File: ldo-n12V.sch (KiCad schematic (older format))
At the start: 0 parts

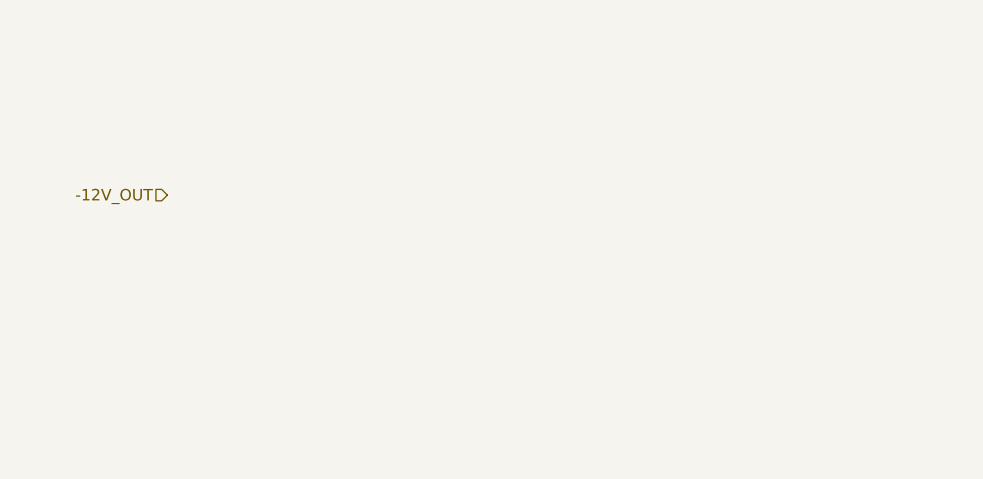
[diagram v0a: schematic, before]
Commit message: add schematics for LDO sheets
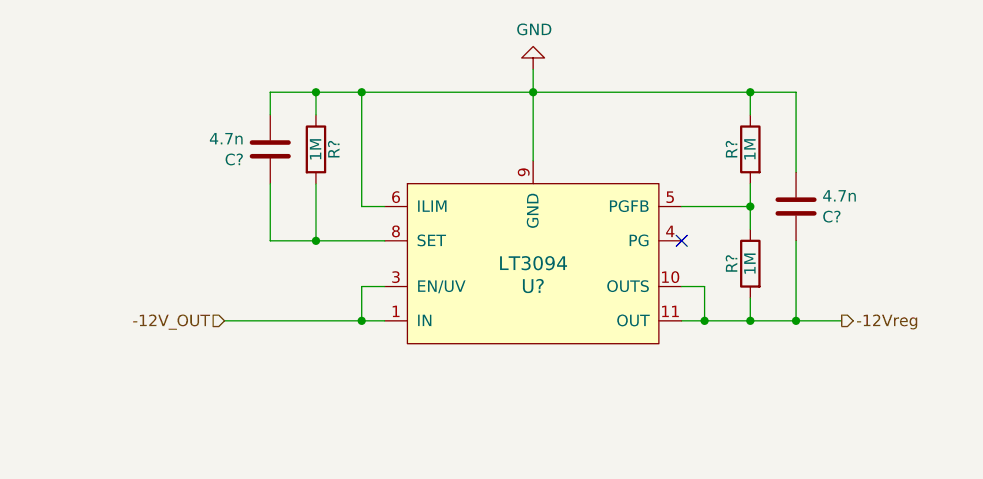
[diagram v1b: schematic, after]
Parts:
- added C? (x2): 4.7n, Capacitor_SMD:C_0805_2012Metric_Pad1.15x1.40mm_HandSolder, symbol Device:C
- added R? (x3): 1M, Resistor_SMD:R_0805_2012Metric_Pad1.15x1.40mm_HandSolder, symbol Device:R
- added U?: LT3094, Housings_SSOP:MSOP-12-1EP_3x4mm_Pitch0.65mm, symbol linear_technology:LT3094
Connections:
- new net: C?.2, R?.2, U?.8 (SET)
- new net: R?.1, R?.2, U?.5 (PGFB)
- new net -12Vreg: C?.2, R?.2, U?.10 (OUTS), U?.11 (OUT), U?.12 (OUT)
- new net GND: C?.1, C?.1, R?.1, R?.1, U?.6 (ILIM), U?.9 (GND)
- new net IN: U?.1 (IN), U?.13 (IN), U?.2 (IN), U?.3 (EN/UV)
- no-connect marks 0 -> 1
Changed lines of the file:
@@
 Comment4 ""
 $EndDescr
-Text HLabel 4300 4150 0    50   Input ~ 0
+Text HLabel 4550 4700 0    50   Input ~ 0
 -12V_OUT
+NoConn ~ 6550 4350
+$Comp
+L power:GND #PWR?
+U 1 1 5CA61EBE
+P 5900 3600
+AR Path="/5C903B7C/5CA61EBE" Ref="#PWR?"  Part="1"
+AR Path="/5CA59CF7/5CA61EBE" Ref="#PWR?"  Part="1"
+F 0 "#PWR?" H 5900 3350 50  0001 C CNN
+F 1 "GND" H 5905 3427 50  0000 C CNN
+F 2 "" H 5900 3600 50  0001 C CNN
+F 3 "" H 5900 3600 50  0001 C CNN
+	1    5900 3600
+	1    0    0    1
+$EndComp
+Wire Wire Line
+	5900 3600 5900 3700
+Wire Wire Line
+	5250 4200 5150 4200
+Wire Wire Line
+	5150 4200 5150 3700
+Wire Wire Line
+	5150 3700 5900 3700
+Connection ~ 5900 3700
+Wire Wire Line
+	5900 3700 5900 4000
+Wire Wire Line
+	4550 4700 5150 4700
+Wire Wire Line
+	5150 4700 5150 4550
+Wire Wire Line
+	5150 4550 5250 4550
+Connection ~ 5150 4700
+Wire Wire Line
+	5150 4700 5250 4700
+$Comp
+L Device:R R?
+U 1 1 5CA61ED4
+P 4950 3950
+AR Path="/5C87B3B6/5CA61ED4" Ref="R?"  Part="1"
+AR Path="/5CA59CF7/5CA61ED4" Ref="R?"  Part="1"
+F 0 "R?" V 5030 3950 50  0000 C CNN
+F 1 "1M" V 4950 3950 50  0000 C CNN
+F 2 "Resistor_SMD:R_0805_2012Metric_Pad1.15x1.40mm_HandSolder" V 4880 3950 50  0001 C CNN
+F 3 "https://industrial.panasonic.com/cdbs/www-data/pdf/RDA0000/AOA0000C304.pdf" H 4950 3950 50  0001 C CNN
+F 4 "RES SMD 1M OHM 1% 1/8W 0805" H 4950 3950 50  0001 C CNN "Description"
+F 5 "Panasonic Electronic Components" H 4950 3950 50  0001 C CNN "Manufacturer"
+F 6 "ERJ-6ENF1004V" H 4950 3950 50  0001 C CNN "Manufacturer Part Number"
+F 7 "Digi-Key" H 4950 3950 50  0001 C CNN "Supplier"
+F 8 "P1.00MCCT-ND" H 4950 3950 50  0001 C CNN "Supplier Part Number"
+	1    4950 3950
+	1    0    0    -1
+$EndComp
+$Comp
+L Device:C C?
+U 1 1 5CA61EE0
+P 4750 3950
+AR Path="/5C87B3B6/5CA61EE0" Ref="C?"  Part="1"
+AR Path="/5CA59CF7/5CA61EE0" Ref="C?"  Part="1"
+F 0 "C?" H 4635 3904 50  0000 R CNN
+F 1 "4.7n" H 4635 3995 50  0000 R CNN
+F 2 "Capacitor_SMD:C_0805_2012Metric_Pad1.15x1.40mm_HandSolder" H 4788 3800 50  0001 C CNN
+F 3 "http://www.samsungsem.com/kr/support/product-search/mlcc/__icsFiles/afieldfile/2018/06/12/CL21C4R7BBANNNC.pdf" H 4750 3950 50  0001 C CNN
+F 4 "CAP CER 4.7PF 50V C0G/NP0 0805" H 2300 -1200 50  0001 C CNN "Description"
+F 5 "Samsung Electro-Mechanics" H 2300 -1200 50  0001 C CNN "Manufacturer"
+F 6 "CL21C4R7BBANNNC" H 2300 -1200 50  0001 C CNN "Manufacturer Part Number"
+F 7 "Digi-Key" H 2300 -1200 50  0001 C CNN "Supplier"
+F 8 "1276-1832-1-ND" H 2300 -1200 50  0001 C CNN "Supplier Part Number"
+	1    4750 3950
+	1    0    0    -1
+$EndComp
+Wire Wire Line
+	5250 4350 4950 4350
+Wire Wire Line
+	4750 4350 4750 4100
+Wire Wire Line
+	4950 4350 4950 4100
+Connection ~ 4950 4350
+Wire Wire Line
+	4950 4350 4750 4350
+Wire Wire Line
+	4750 3800 4750 3700
+Wire Wire Line
+	4750 3700 4950 3700
+Connection ~ 5150 3700
+Wire Wire Line
+	4950 3800 4950 3700
+Connection ~ 4950 3700
+Wire Wire Line
+	4950 3700 5150 3700
+$Comp
+L Device:R R?
+U 1 1 5CA61EF7
+P 6850 3950
+AR Path="/5C87B3B6/5CA61EF7" Ref="R?"  Part="1"
+AR Path="/5CA59CF7/5CA61EF7" Ref="R?"  Part="1"
+F 0 "R?" V 6930 3950 50  0000 C CNN
+F 1 "1M" V 6850 3950 50  0000 C CNN
+F 2 "Resistor_SMD:R_0805_2012Metric_Pad1.15x1.40mm_HandSolder" V 6780 3950 50  0001 C CNN
+F 3 "https://industrial.panasonic.com/cdbs/www-data/pdf/RDA0000/AOA0000C304.pdf" H 6850 3950 50  0001 C CNN
+F 4 "RES SMD 1M OHM 1% 1/8W 0805" H 6850 3950 50  0001 C CNN "Description"
+F 5 "Panasonic Electronic Components" H 6850 3950 50  0001 C CNN "Manufacturer"
+F 6 "ERJ-6ENF1004V" H 6850 3950 50  0001 C CNN "Manufacturer Part Number"
+F 7 "Digi-Key" H 6850 3950 50  0001 C CNN "Supplier"
+F 8 "P1.00MCCT-ND" H 6850 3950 50  0001 C CNN "Supplier Part Number"
+	1    6850 3950
+	-1   0    0    -1
+$EndComp
+$Comp
+L Device:R R?
+U 1 1 5CA61F03
+P 6850 4450
+AR Path="/5C87B3B6/5CA61F03" Ref="R?"  Part="1"
+AR Path="/5CA59CF7/5CA61F03" Ref="R?"  Part="1"
+F 0 "R?" V 6930 4450 50  0000 C CNN
+F 1 "1M" V 6850 4450 50  0000 C CNN
+F 2 "Resistor_SMD:R_0805_2012Metric_Pad1.15x1.40mm_HandSolder" V 6780 4450 50  0001 C CNN
+F 3 "https://industrial.panasonic.com/cdbs/www-data/pdf/RDA0000/AOA0000C304.pdf" H 6850 4450 50  0001 C CNN
+F 4 "RES SMD 1M OHM 1% 1/8W 0805" H 6850 4450 50  0001 C CNN "Description"
+F 5 "Panasonic Electronic Components" H 6850 4450 50  0001 C CNN "Manufacturer"
+F 6 "ERJ-6ENF1004V" H 6850 4450 50  0001 C CNN "Manufacturer Part Number"
+F 7 "Digi-Key" H 6850 4450 50  0001 C CNN "Supplier"
+F 8 "P1.00MCCT-ND" H 6850 4450 50  0001 C CNN "Supplier Part Number"
+	1    6850 4450
+	-1   0    0    -1
+$EndComp
+Wire Wire Line
+	6550 4200 6850 4200
+Wire Wire Line
+	6850 4200 6850 4300
+Wire Wire Line
+	6550 4700 6650 4700
+Wire Wire Line
+	6850 4700 6850 4600
+Wire Wire Line
+	6550 4550 6650 4550
+Wire Wire Line
+	6650 4550 6650 4700
+Connection ~ 6650 4700
+Wire Wire Line
+	6650 4700 6850 4700
+Wire Wire Line
+	6850 4200 6850 4100
+Connection ~ 6850 4200
+Wire Wire Line
+	6850 3800 6850 3700
+Wire Wire Line
+	6850 3700 5900 3700
+$Comp
+L Device:C C?
+U 1 1 5CA61F1B
+P 7050 4200
+AR Path="/5C87B3B6/5CA61F1B" Ref="C?"  Part="1"
+AR Path="/5CA59CF7/5CA61F1B" Ref="C?"  Part="1"
+F 0 "C?" H 6935 4154 50  0000 R CNN
+F 1 "4.7n" H 6935 4245 50  0000 R CNN
+F 2 "Capacitor_SMD:C_0805_2012Metric_Pad1.15x1.40mm_HandSolder" H 7088 4050 50  0001 C CNN
+F 3 "http://www.samsungsem.com/kr/support/product-search/mlcc/__icsFiles/afieldfile/2018/06/12/CL21C4R7BBANNNC.pdf" H 7050 4200 50  0001 C CNN
+F 4 "CAP CER 4.7PF 50V C0G/NP0 0805" H 4600 -950 50  0001 C CNN "Description"
+F 5 "Samsung Electro-Mechanics" H 4600 -950 50  0001 C CNN "Manufacturer"
+F 6 "CL21C4R7BBANNNC" H 4600 -950 50  0001 C CNN "Manufacturer Part Number"
+F 7 "Digi-Key" H 4600 -950 50  0001 C CNN "Supplier"
+F 8 "1276-1832-1-ND" H 4600 -950 50  0001 C CNN "Supplier Part Number"
+	1    7050 4200
+	-1   0    0    -1
+$EndComp
+Wire Wire Line
+	6850 4700 7050 4700
+Wire Wire Line
+	7050 4700 7050 4350
+Connection ~ 6850 4700
+Wire Wire Line
+	7050 4050 7050 3700
+Wire Wire Line
+	7050 3700 6850 3700
+Connection ~ 6850 3700
+Text HLabel 7250 4700 2    50   Output ~ 0
+-12Vreg
+Wire Wire Line
+	7250 4700 7050 4700
+Connection ~ 7050 4700
+$Comp
+L linear_technology:LT3094 U?
+U 1 1 5CA624E4
+P 5900 4450
+F 0 "U?" H 5900 4350 60  0000 C CNN
+F 1 "LT3094" H 5900 4450 60  0000 C CNN
+F 2 "Housings_SSOP:MSOP-12-1EP_3x4mm_Pitch0.65mm" H 5900 3950 60  0001 C CNN
+F 3 "https://www.analog.com/media/en/technical-documentation/data-sheets/LT3094.pdf" H 5900 4050 60  0001 C CNN
+	1    5900 4450
+	1    0    0    -1
+$EndComp
 $EndSCHEMATC

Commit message: update schematic after LTSpice simulations
- enable EN/UV and PGFB usage for LDOs
  - PGFB required for fast startup
  - EN/UV required to allow boost to ramp up
- take care of some TODOs in usbc-power sch
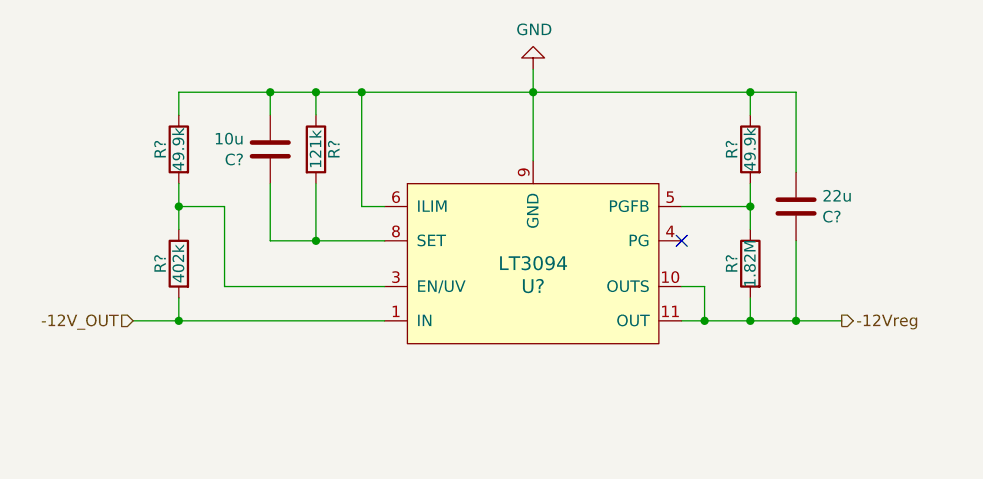
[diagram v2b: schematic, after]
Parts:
- added R?: 49.9k, Resistor_SMD:R_0805_2012Metric_Pad1.15x1.40mm_HandSolder, symbol Device:R
- added R?: 402k, Resistor_SMD:R_0805_2012Metric_Pad1.15x1.40mm_HandSolder, symbol Device:R
- C?: value 4.7n -> 10u
- C?: value 4.7n -> 22u
- R?: value 1M -> 121k
- R?: value 1M -> 49.9k
- R?: value 1M -> 1.82M
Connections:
- net GND: now also R?.1
- net IN: now also R?.2; no longer U?.3 (EN/UV)
- new net: R?.1, R?.2, U?.3 (EN/UV)
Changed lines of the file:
@@
 Comment4 ""
 $EndDescr
-Text HLabel 4550 4700 0    50   Input ~ 0
+Text HLabel 4150 4700 0    50   Input ~ 0
 -12V_OUT
 NoConn ~ 6550 4350
@@
 AR Path="/5C903B7C/5CA61EBE" Ref="#PWR?"  Part="1"
 AR Path="/5CA59CF7/5CA61EBE" Ref="#PWR?"  Part="1"
+AR Path="/5CA59CFA/5CA61EBE" Ref="#PWR?"  Part="1"
 F 0 "#PWR?" H 5900 3350 50  0001 C CNN
 F 1 "GND" H 5905 3427 50  0000 C CNN
@@
 Wire Wire Line
 	5900 3700 5900 4000
-Wire Wire Line
-	4550 4700 5150 4700
-Wire Wire Line
-	5150 4700 5150 4550
-Wire Wire Line
-	5150 4550 5250 4550
-Connection ~ 5150 4700
-Wire Wire Line
-	5150 4700 5250 4700
 $Comp
 L Device:R R?
@@
 AR Path="/5C87B3B6/5CA61ED4" Ref="R?"  Part="1"
 AR Path="/5CA59CF7/5CA61ED4" Ref="R?"  Part="1"
+AR Path="/5CA59CFA/5CA61ED4" Ref="R?"  Part="1"
 F 0 "R?" V 5030 3950 50  0000 C CNN
-F 1 "1M" V 4950 3950 50  0000 C CNN
+F 1 "121k" V 4950 3950 50  0000 C CNN
 F 2 "Resistor_SMD:R_0805_2012Metric_Pad1.15x1.40mm_HandSolder" V 4880 3950 50  0001 C CNN
 F 3 "https://industrial.panasonic.com/cdbs/www-data/pdf/RDA0000/AOA0000C304.pdf" H 4950 3950 50  0001 C CNN
@@
 AR Path="/5C87B3B6/5CA61EE0" Ref="C?"  Part="1"
 AR Path="/5CA59CF7/5CA61EE0" Ref="C?"  Part="1"
+AR Path="/5CA59CFA/5CA61EE0" Ref="C?"  Part="1"
 F 0 "C?" H 4635 3904 50  0000 R CNN
-F 1 "4.7n" H 4635 3995 50  0000 R CNN
+F 1 "10u" H 4635 3995 50  0000 R CNN
 F 2 "Capacitor_SMD:C_0805_2012Metric_Pad1.15x1.40mm_HandSolder" H 4788 3800 50  0001 C CNN
 F 3 "http://www.samsungsem.com/kr/support/product-search/mlcc/__icsFiles/afieldfile/2018/06/12/CL21C4R7BBANNNC.pdf" H 4750 3950 50  0001 C CNN
@@
 AR Path="/5C87B3B6/5CA61EF7" Ref="R?"  Part="1"
 AR Path="/5CA59CF7/5CA61EF7" Ref="R?"  Part="1"
+AR Path="/5CA59CFA/5CA61EF7" Ref="R?"  Part="1"
 F 0 "R?" V 6930 3950 50  0000 C CNN
-F 1 "1M" V 6850 3950 50  0000 C CNN
+F 1 "49.9k" V 6850 3950 50  0000 C CNN
 F 2 "Resistor_SMD:R_0805_2012Metric_Pad1.15x1.40mm_HandSolder" V 6780 3950 50  0001 C CNN
 F 3 "https://industrial.panasonic.com/cdbs/www-data/pdf/RDA0000/AOA0000C304.pdf" H 6850 3950 50  0001 C CNN
@@
 AR Path="/5C87B3B6/5CA61F03" Ref="R?"  Part="1"
 AR Path="/5CA59CF7/5CA61F03" Ref="R?"  Part="1"
+AR Path="/5CA59CFA/5CA61F03" Ref="R?"  Part="1"
 F 0 "R?" V 6930 4450 50  0000 C CNN
-F 1 "1M" V 6850 4450 50  0000 C CNN
+F 1 "1.82M" V 6850 4450 50  0000 C CNN
 F 2 "Resistor_SMD:R_0805_2012Metric_Pad1.15x1.40mm_HandSolder" V 6780 4450 50  0001 C CNN
 F 3 "https://industrial.panasonic.com/cdbs/www-data/pdf/RDA0000/AOA0000C304.pdf" H 6850 4450 50  0001 C CNN
@@
 AR Path="/5C87B3B6/5CA61F1B" Ref="C?"  Part="1"
 AR Path="/5CA59CF7/5CA61F1B" Ref="C?"  Part="1"
+AR Path="/5CA59CFA/5CA61F1B" Ref="C?"  Part="1"
 F 0 "C?" H 6935 4154 50  0000 R CNN
-F 1 "4.7n" H 6935 4245 50  0000 R CNN
+F 1 "22u" H 6935 4245 50  0000 R CNN
 F 2 "Capacitor_SMD:C_0805_2012Metric_Pad1.15x1.40mm_HandSolder" H 7088 4050 50  0001 C CNN
 F 3 "http://www.samsungsem.com/kr/support/product-search/mlcc/__icsFiles/afieldfile/2018/06/12/CL21C4R7BBANNNC.pdf" H 7050 4200 50  0001 C CNN
@@
 	1    0    0    -1
 $EndComp
+$Comp
+L Device:R R?
+U 1 1 5CAC362A
+P 4350 3950
+AR Path="/5C87B3B6/5CAC362A" Ref="R?"  Part="1"
+AR Path="/5CA59CF7/5CAC362A" Ref="R?"  Part="1"
+AR Path="/5CA59CFA/5CAC362A" Ref="R?"  Part="1"
+F 0 "R?" V 4430 3950 50  0000 C CNN
+F 1 "49.9k" V 4350 3950 50  0000 C CNN
+F 2 "Resistor_SMD:R_0805_2012Metric_Pad1.15x1.40mm_HandSolder" V 4280 3950 50  0001 C CNN
+F 3 "https://industrial.panasonic.com/cdbs/www-data/pdf/RDA0000/AOA0000C304.pdf" H 4350 3950 50  0001 C CNN
+F 4 "RES SMD 1M OHM 1% 1/8W 0805" H 4350 3950 50  0001 C CNN "Description"
+F 5 "Panasonic Electronic Components" H 4350 3950 50  0001 C CNN "Manufacturer"
+F 6 "ERJ-6ENF1004V" H 4350 3950 50  0001 C CNN "Manufacturer Part Number"
+F 7 "Digi-Key" H 4350 3950 50  0001 C CNN "Supplier"
+F 8 "P1.00MCCT-ND" H 4350 3950 50  0001 C CNN "Supplier Part Number"
+	1    4350 3950
+	-1   0    0    -1
+$EndComp
+$Comp
+L Device:R R?
+U 1 1 5CAC3636
+P 4350 4450
+AR Path="/5C87B3B6/5CAC3636" Ref="R?"  Part="1"
+AR Path="/5CA59CF7/5CAC3636" Ref="R?"  Part="1"
+AR Path="/5CA59CFA/5CAC3636" Ref="R?"  Part="1"
+F 0 "R?" V 4430 4450 50  0000 C CNN
+F 1 "402k" V 4350 4450 50  0000 C CNN
+F 2 "Resistor_SMD:R_0805_2012Metric_Pad1.15x1.40mm_HandSolder" V 4280 4450 50  0001 C CNN
+F 3 "https://industrial.panasonic.com/cdbs/www-data/pdf/RDA0000/AOA0000C304.pdf" H 4350 4450 50  0001 C CNN
+F 4 "RES SMD 1M OHM 1% 1/8W 0805" H 4350 4450 50  0001 C CNN "Description"
+F 5 "Panasonic Electronic Components" H 4350 4450 50  0001 C CNN "Manufacturer"
+F 6 "ERJ-6ENF1004V" H 4350 4450 50  0001 C CNN "Manufacturer Part Number"
+F 7 "Digi-Key" H 4350 4450 50  0001 C CNN "Supplier"
+F 8 "P1.00MCCT-ND" H 4350 4450 50  0001 C CNN "Supplier Part Number"
+	1    4350 4450
+	-1   0    0    -1
+$EndComp
+Wire Wire Line
+	4350 4700 4350 4600
+Wire Wire Line
+	4350 3800 4350 3700
+Wire Wire Line
+	4150 4700 4350 4700
+Wire Wire Line
+	4350 4700 5250 4700
+Connection ~ 4350 4700
+Wire Wire Line
+	4350 4100 4350 4200
+Wire Wire Line
+	5250 4550 4550 4550
+Wire Wire Line
+	4550 4550 4550 4200
+Wire Wire Line
+	4550 4200 4350 4200
+Connection ~ 4350 4200
+Wire Wire Line
+	4350 4200 4350 4300
+Wire Wire Line
+	4350 3700 4750 3700
+Connection ~ 4750 3700
 $EndSCHEMATC

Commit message: remove false desc for copied resistors in ldo schematics
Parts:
- C? (x2): Description CAP CER 4.7PF 50V C0G/NP0 0805 -> (none)
- R? (x5): Description RES SMD 1M OHM 1% 1/8W 0805 -> (none)
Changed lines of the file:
@@
 F 2 "Resistor_SMD:R_0805_2012Metric_Pad1.15x1.40mm_HandSolder" V 4880 3950 50  0001 C CNN
 F 3 "https://industrial.panasonic.com/cdbs/www-data/pdf/RDA0000/AOA0000C304.pdf" H 4950 3950 50  0001 C CNN
-F 4 "RES SMD 1M OHM 1% 1/8W 0805" H 4950 3950 50  0001 C CNN "Description"
+F 4 "" H 4950 3950 50  0001 C CNN "Description"
 F 5 "Panasonic Electronic Components" H 4950 3950 50  0001 C CNN "Manufacturer"
 F 6 "ERJ-6ENF1004V" H 4950 3950 50  0001 C CNN "Manufacturer Part Number"
@@
 F 2 "Capacitor_SMD:C_0805_2012Metric_Pad1.15x1.40mm_HandSolder" H 4788 3800 50  0001 C CNN
 F 3 "http://www.samsungsem.com/kr/support/product-search/mlcc/__icsFiles/afieldfile/2018/06/12/CL21C4R7BBANNNC.pdf" H 4750 3950 50  0001 C CNN
-F 4 "CAP CER 4.7PF 50V C0G/NP0 0805" H 2300 -1200 50  0001 C CNN "Description"
+F 4 "" H 2300 -1200 50  0001 C CNN "Description"
 F 5 "Samsung Electro-Mechanics" H 2300 -1200 50  0001 C CNN "Manufacturer"
 F 6 "CL21C4R7BBANNNC" H 2300 -1200 50  0001 C CNN "Manufacturer Part Number"
@@
 F 2 "Resistor_SMD:R_0805_2012Metric_Pad1.15x1.40mm_HandSolder" V 6780 3950 50  0001 C CNN
 F 3 "https://industrial.panasonic.com/cdbs/www-data/pdf/RDA0000/AOA0000C304.pdf" H 6850 3950 50  0001 C CNN
-F 4 "RES SMD 1M OHM 1% 1/8W 0805" H 6850 3950 50  0001 C CNN "Description"
+F 4 "" H 6850 3950 50  0001 C CNN "Description"
 F 5 "Panasonic Electronic Components" H 6850 3950 50  0001 C CNN "Manufacturer"
 F 6 "ERJ-6ENF1004V" H 6850 3950 50  0001 C CNN "Manufacturer Part Number"
@@
 F 2 "Resistor_SMD:R_0805_2012Metric_Pad1.15x1.40mm_HandSolder" V 6780 4450 50  0001 C CNN
 F 3 "https://industrial.panasonic.com/cdbs/www-data/pdf/RDA0000/AOA0000C304.pdf" H 6850 4450 50  0001 C CNN
-F 4 "RES SMD 1M OHM 1% 1/8W 0805" H 6850 4450 50  0001 C CNN "Description"
+F 4 "" H 6850 4450 50  0001 C CNN "Description"
 F 5 "Panasonic Electronic Components" H 6850 4450 50  0001 C CNN "Manufacturer"
 F 6 "ERJ-6ENF1004V" H 6850 4450 50  0001 C CNN "Manufacturer Part Number"
@@
 F 2 "Capacitor_SMD:C_0805_2012Metric_Pad1.15x1.40mm_HandSolder" H 7088 4050 50  0001 C CNN
 F 3 "http://www.samsungsem.com/kr/support/product-search/mlcc/__icsFiles/afieldfile/2018/06/12/CL21C4R7BBANNNC.pdf" H 7050 4200 50  0001 C CNN
-F 4 "CAP CER 4.7PF 50V C0G/NP0 0805" H 4600 -950 50  0001 C CNN "Description"
+F 4 "" H 4600 -950 50  0001 C CNN "Description"
 F 5 "Samsung Electro-Mechanics" H 4600 -950 50  0001 C CNN "Manufacturer"
 F 6 "CL21C4R7BBANNNC" H 4600 -950 50  0001 C CNN "Manufacturer Part Number"
@@
 F 2 "Resistor_SMD:R_0805_2012Metric_Pad1.15x1.40mm_HandSolder" V 4280 3950 50  0001 C CNN
 F 3 "https://industrial.panasonic.com/cdbs/www-data/pdf/RDA0000/AOA0000C304.pdf" H 4350 3950 50  0001 C CNN
-F 4 "RES SMD 1M OHM 1% 1/8W 0805" H 4350 3950 50  0001 C CNN "Description"
+F 4 "" H 4350 3950 50  0001 C CNN "Description"
 F 5 "Panasonic Electronic Components" H 4350 3950 50  0001 C CNN "Manufacturer"
 F 6 "ERJ-6ENF1004V" H 4350 3950 50  0001 C CNN "Manufacturer Part Number"
@@
 F 2 "Resistor_SMD:R_0805_2012Metric_Pad1.15x1.40mm_HandSolder" V 4280 4450 50  0001 C CNN
 F 3 "https://industrial.panasonic.com/cdbs/www-data/pdf/RDA0000/AOA0000C304.pdf" H 4350 4450 50  0001 C CNN
-F 4 "RES SMD 1M OHM 1% 1/8W 0805" H 4350 4450 50  0001 C CNN "Description"
+F 4 "" H 4350 4450 50  0001 C CNN "Description"
 F 5 "Panasonic Electronic Components" H 4350 4450 50  0001 C CNN "Manufacturer"
 F 6 "ERJ-6ENF1004V" H 4350 4450 50  0001 C CNN "Manufacturer Part Number"

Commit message: update hierarchal pin names to be accurate to new settings
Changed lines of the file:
@@
 $EndDescr
 Text HLabel 4150 4700 0    50   Input ~ 0
--12V_OUT
+-13V_IN
 NoConn ~ 6550 4350
 $Comp
